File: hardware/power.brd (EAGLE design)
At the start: 50 x 50 mm, 36 parts, among them U1 LM324D, U2 LM324D, U3 LM1117MP-3.3

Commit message: cleaned up placement print
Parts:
- moved TEMP-1 18.5 mm to (17.8, 27.9)
- moved OFFSET-1 5.08 mm to (10.2, 35.6)
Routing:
- net TEMP_1: track 34.1 -> 30.1 mm
- net OFFSET_1: track 21.8 -> 20.7 mm

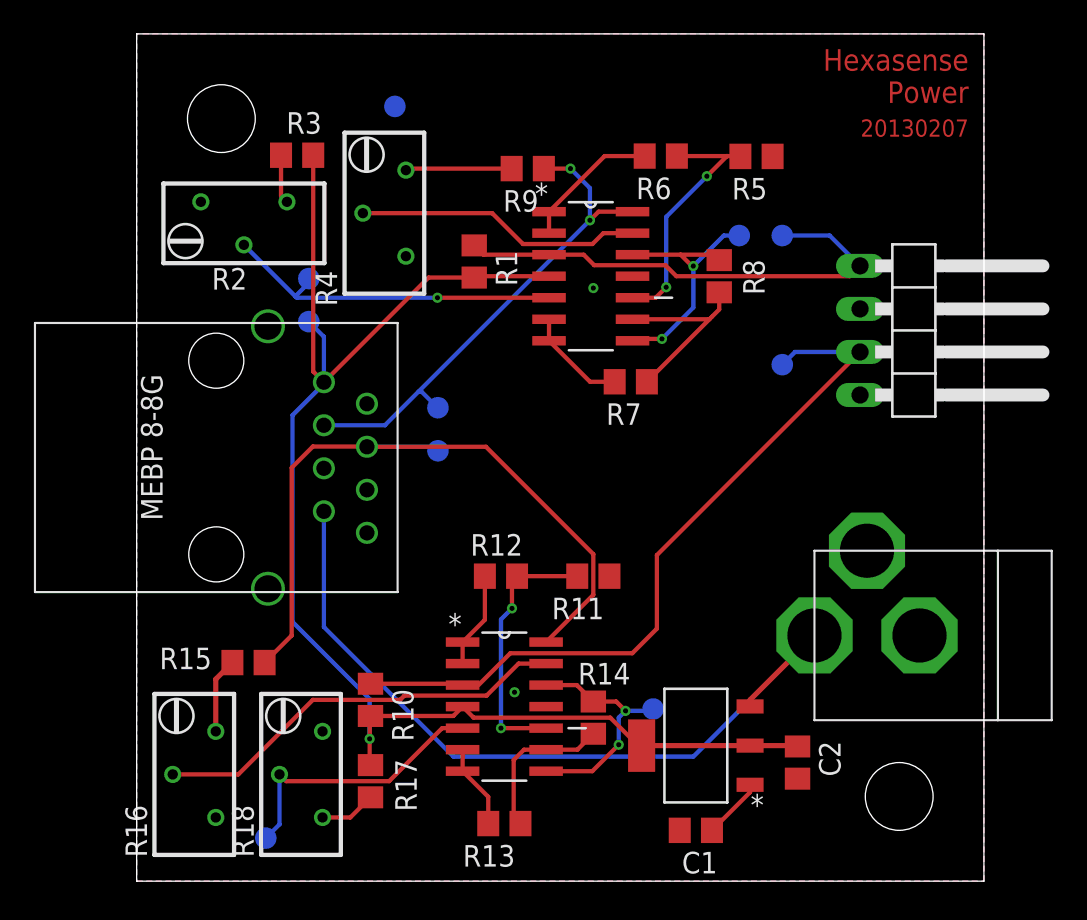
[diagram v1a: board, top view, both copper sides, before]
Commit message: changed testpads to THT
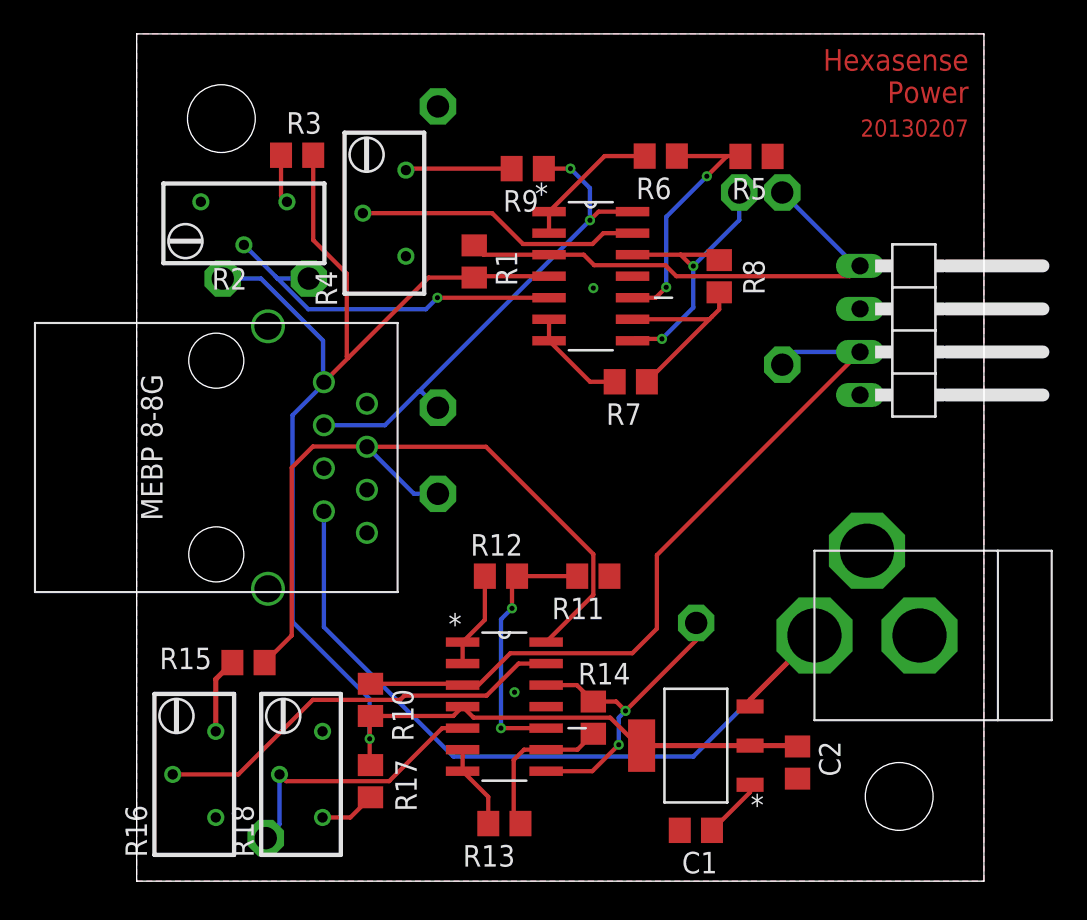
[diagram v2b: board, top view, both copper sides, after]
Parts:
- GND, OFFSET-1, OFFSET-2, PT100-1, PT100-2, TEMP-1, TEMP-2, U_M-1, U_M-2, VCC: value TPB1,27 -> TPPAD1-13; device testpad:B1,27 -> testpad:P1-13
- moved U_M-2 5.68 mm to (33.0, 15.2)
- moved VCC 5.68 mm to (5.08, 35.6), turned to 270 degrees
- moved GND 2.54 mm to (17.8, 45.7)
- moved PT100-1 2.54 mm to (38.1, 40.6)
- moved TEMP-2 2.54 mm to (17.8, 22.9)
- moved U_M-1 2.54 mm to (35.6, 40.6)
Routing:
- net U_M_2: track 14.1 -> 19.3 mm
- net +3V3: track 86.5 -> 91.6 mm
- net U_M_1: track 16.6 -> 18.6 mm
- net PT100_1: track 29.1 -> 30.2 mm
- net TEMP_2: track 43.7 -> 44.8 mm
- net OFFSET_1: track 20.7 -> 21.7 mm
